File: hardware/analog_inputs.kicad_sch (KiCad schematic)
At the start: 46 parts, among them U2 MCP6N11-005, U3 MCP6N11-005, U4 MCP6001, U5 MCP6001

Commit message: Refactor
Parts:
- R15, R17: value TBD -> 6k
- R16, R18: value TBD -> 1k
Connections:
- net SENSOR1 renamed OUT1
- net SENSOR2 renamed OUT2
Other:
- note added: "G = 7"
- note removed: "G = TBD"

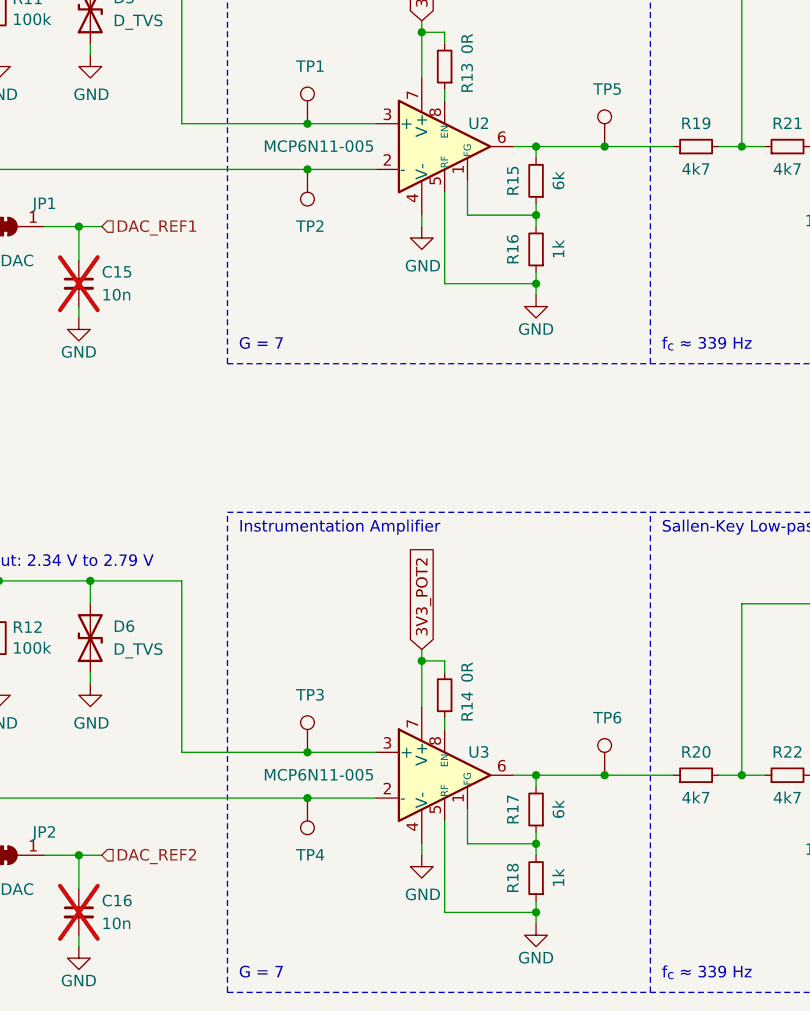
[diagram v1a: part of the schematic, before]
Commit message: Update component values
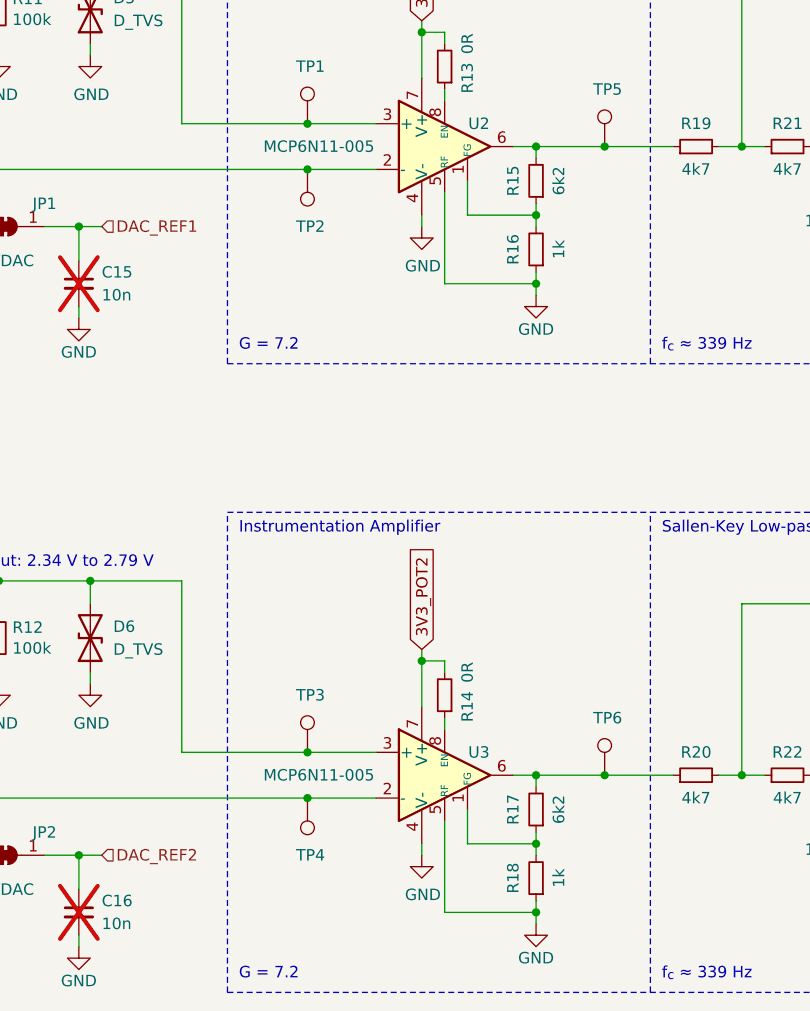
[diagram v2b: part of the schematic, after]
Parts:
- R15, R17: value 6k -> 6k2
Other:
- note added: "G = 7.2"
- note removed: "G = 7"
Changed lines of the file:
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@@
     (effects (font (size 1.27 1.27)) (justify right bottom))
   )
-  (text "G = 7" (at 140.97 152.4 0)
+  (text "G = 7.2" (at 140.97 152.4 0)
     (effects (font (size 1.27 1.27)) (justify left bottom))
   )
@@
     (effects (font (size 1.27 1.27)) (justify left bottom))
   )
-  (text "G = 7" (at 140.97 82.55 0)
+  (text "G = 7.2" (at 140.97 82.55 0)
     (effects (font (size 1.27 1.27)) (justify left bottom))
   )
@@
       (effects (font (size 1.27 1.27)))
     )
-    (property "Value" "6k" (at 176.53 133.35 90)
+    (property "Value" "6k2" (at 176.53 133.35 90)
       (effects (font (size 1.27 1.27)))
     )
@@
       (effects (font (size 1.27 1.27)))
     )
-    (property "Value" "6k" (at 176.53 63.5 90)
-      (effects (font (size 1.27 1.27)))
-    )
+    (property "Value" "6k2" (at 176.53 63.5 90)
+      (effects (font (size 1.27 1.27)))
+    )

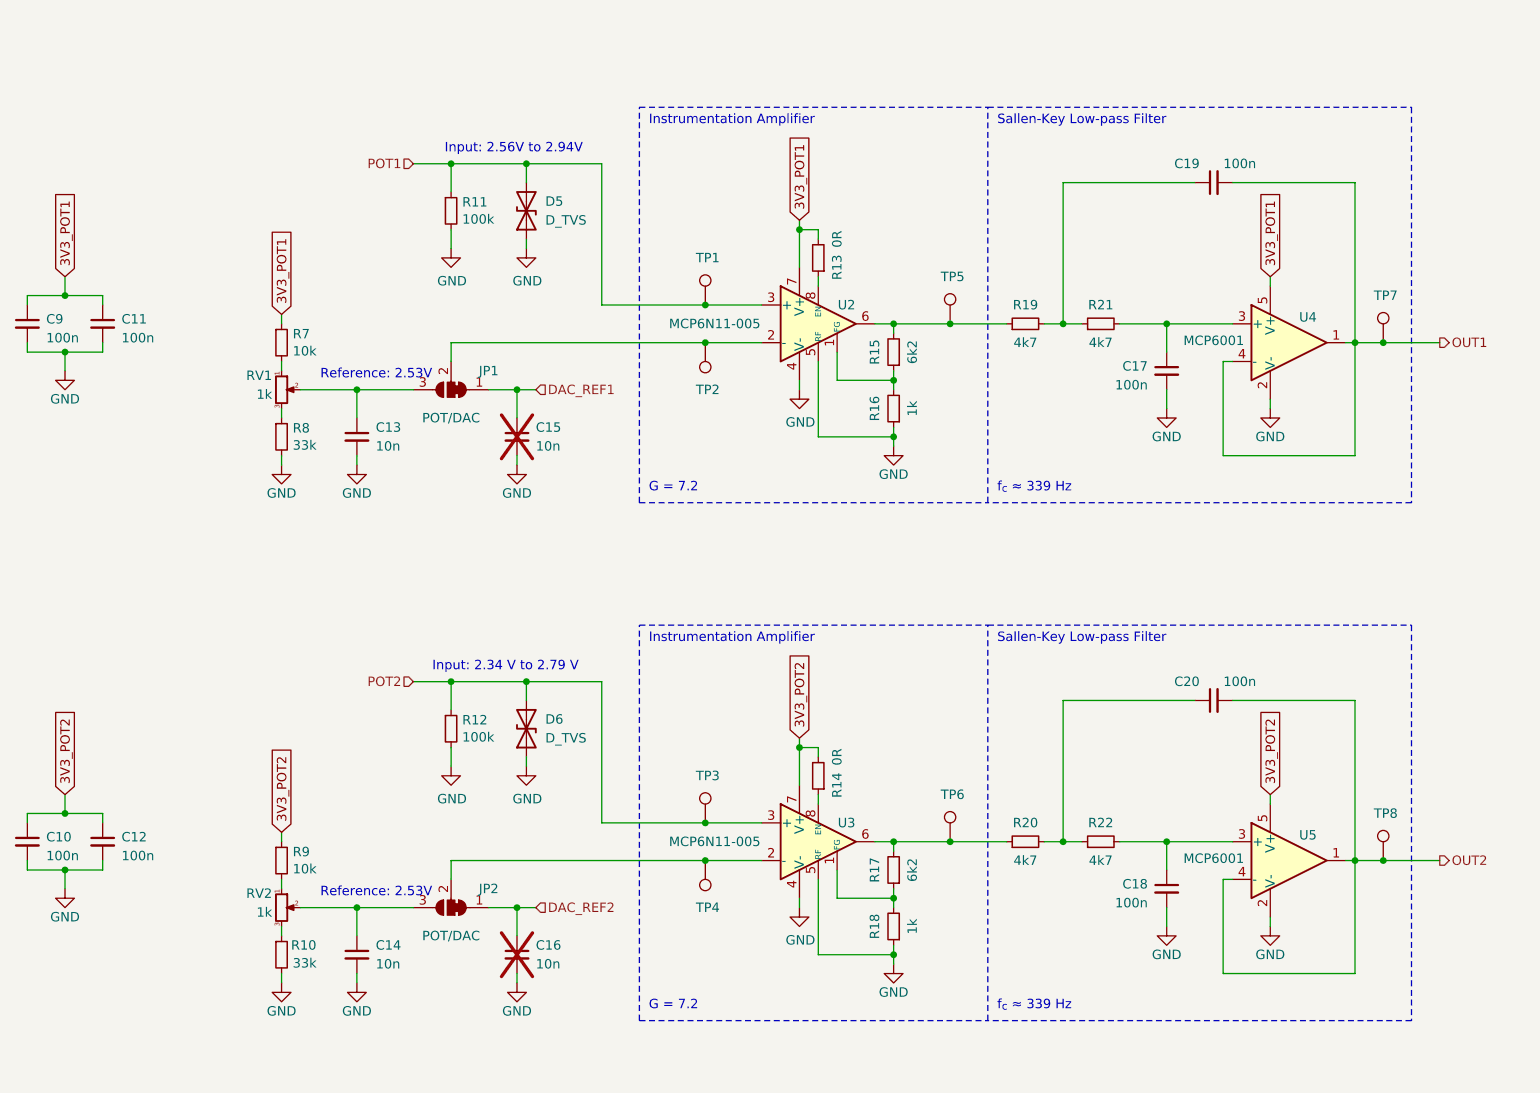
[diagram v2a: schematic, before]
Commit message: Adjust component values
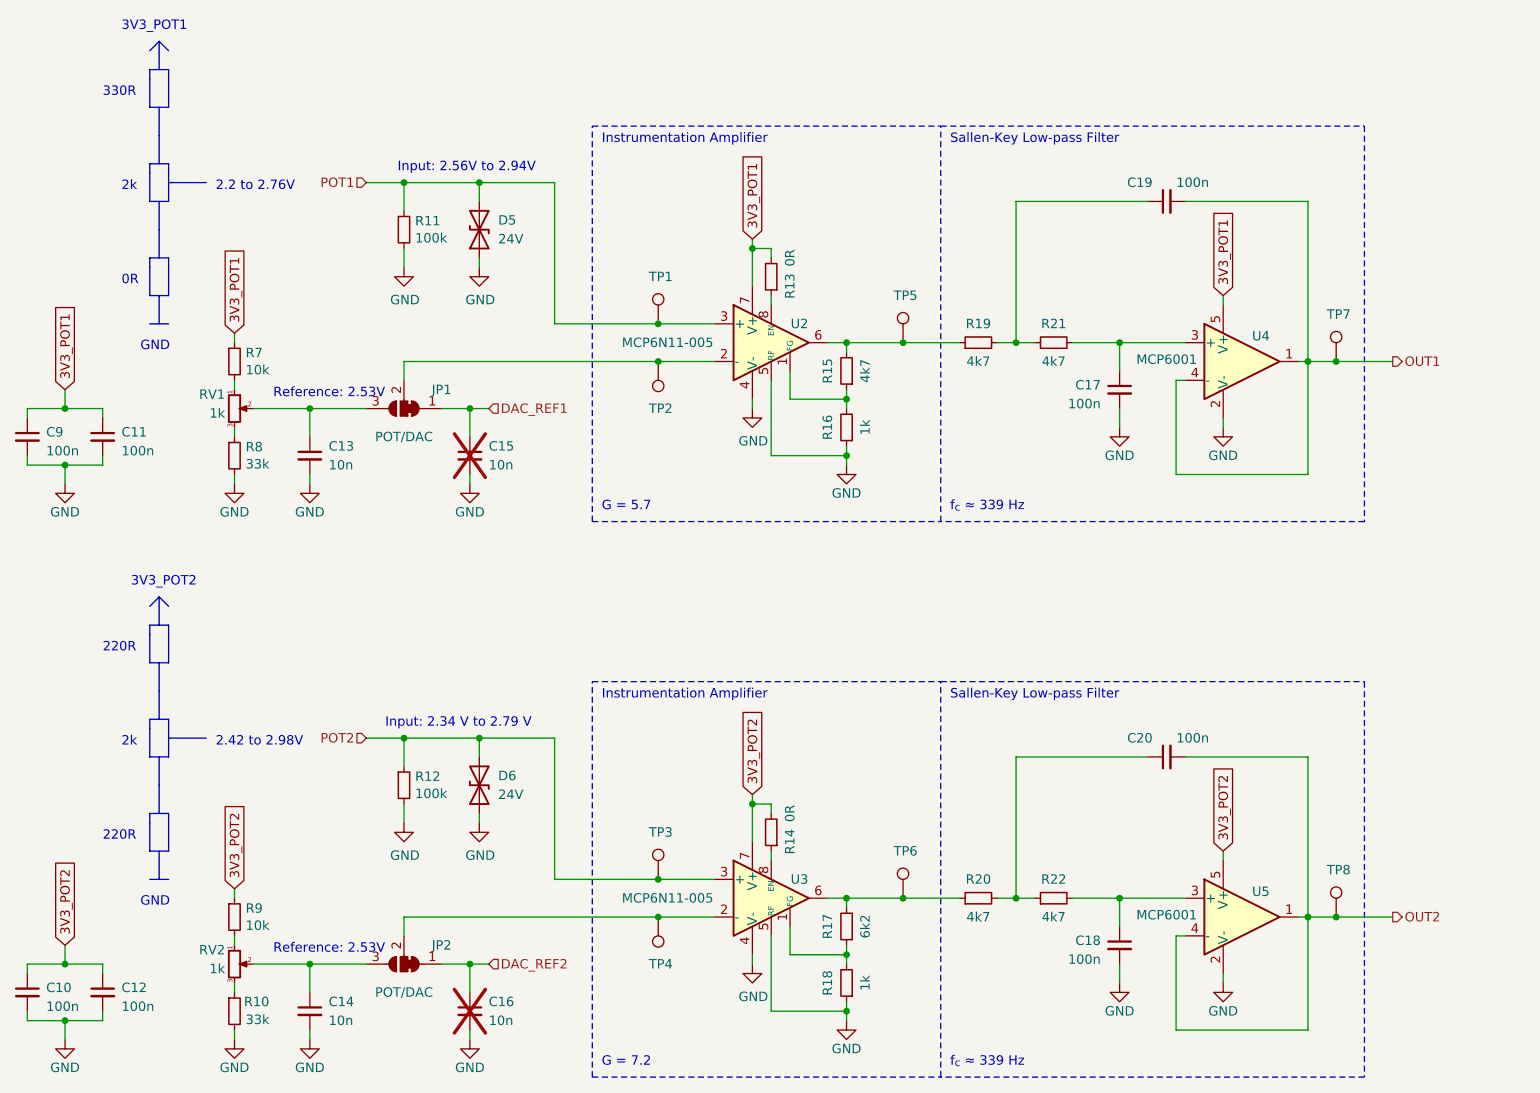
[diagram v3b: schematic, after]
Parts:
- D5, D6: value D_TVS -> 24V
- R15: value 6k2 -> 4k7
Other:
- note added: "0R"
- note added: "2.2 to 2.76V"
- note added: "2.42 to 2.98V"
- note added: "220R"
- note added: "2k"
- note added: "330R"
- note added: "3V3_POT1"
- note added: "3V3_POT2"
- note added: "G = 5.7"
- note added: "GND"
- moved on the sheet: C10, C11, C12, C13, C14, C15, C16, C17, C18, C19, C20, C9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
